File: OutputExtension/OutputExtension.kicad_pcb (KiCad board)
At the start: 2 copper layers, 34 parts, among them P1 CONN_01X04, P2 CONN_01X04, P3 CONN_01X04, P4 CONN_01X08, P5 CONN_01X08, Q1 IRL640, Q2 IRL640, Q3 IRL640, Q4 IRL640, Q5 IRL640, Q6 IRL640, Q7 IRL640, Q8 IRL640, U1 PCF8574

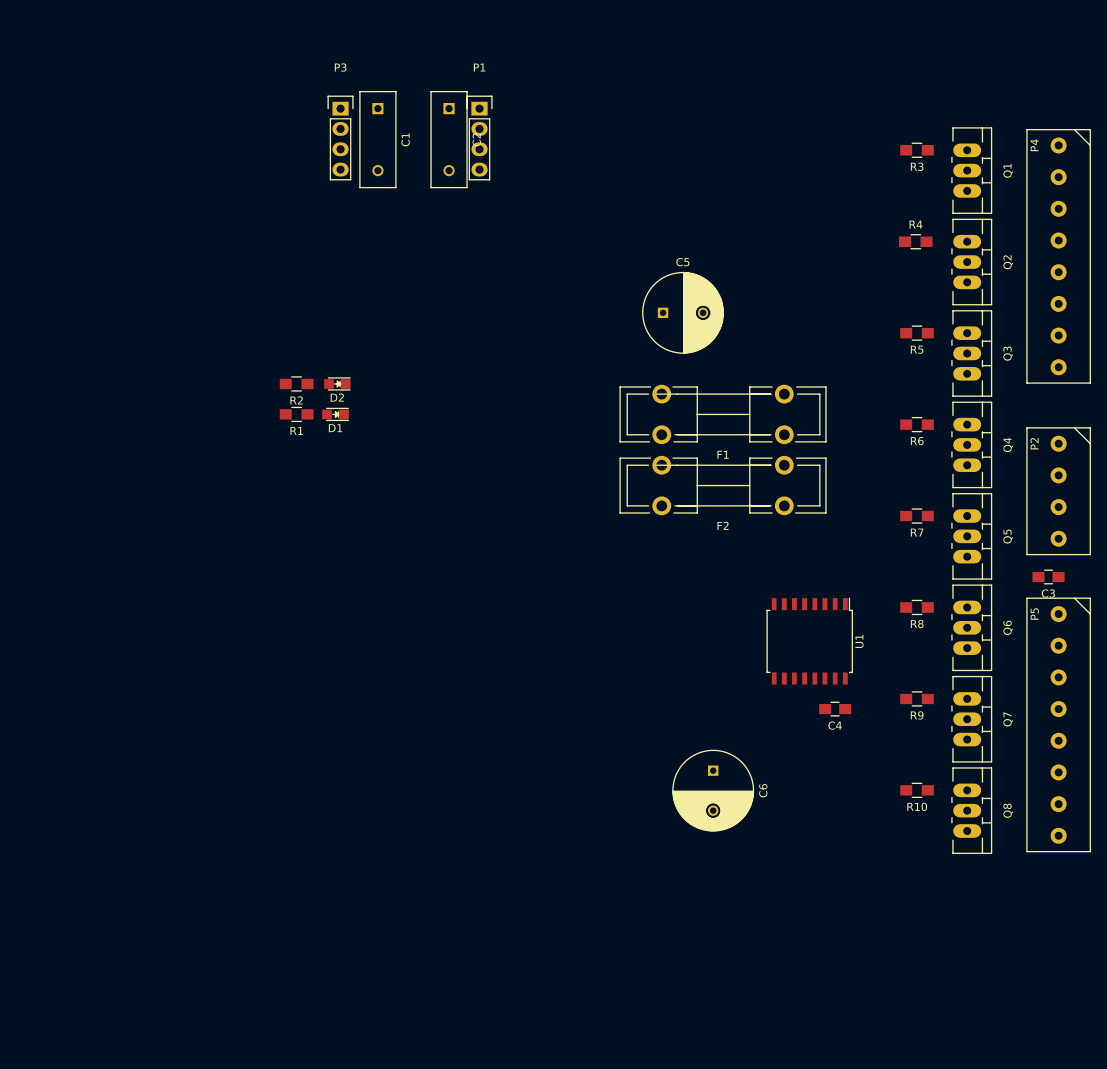
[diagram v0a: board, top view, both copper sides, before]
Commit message: Output extension looks good. Diodes still missing
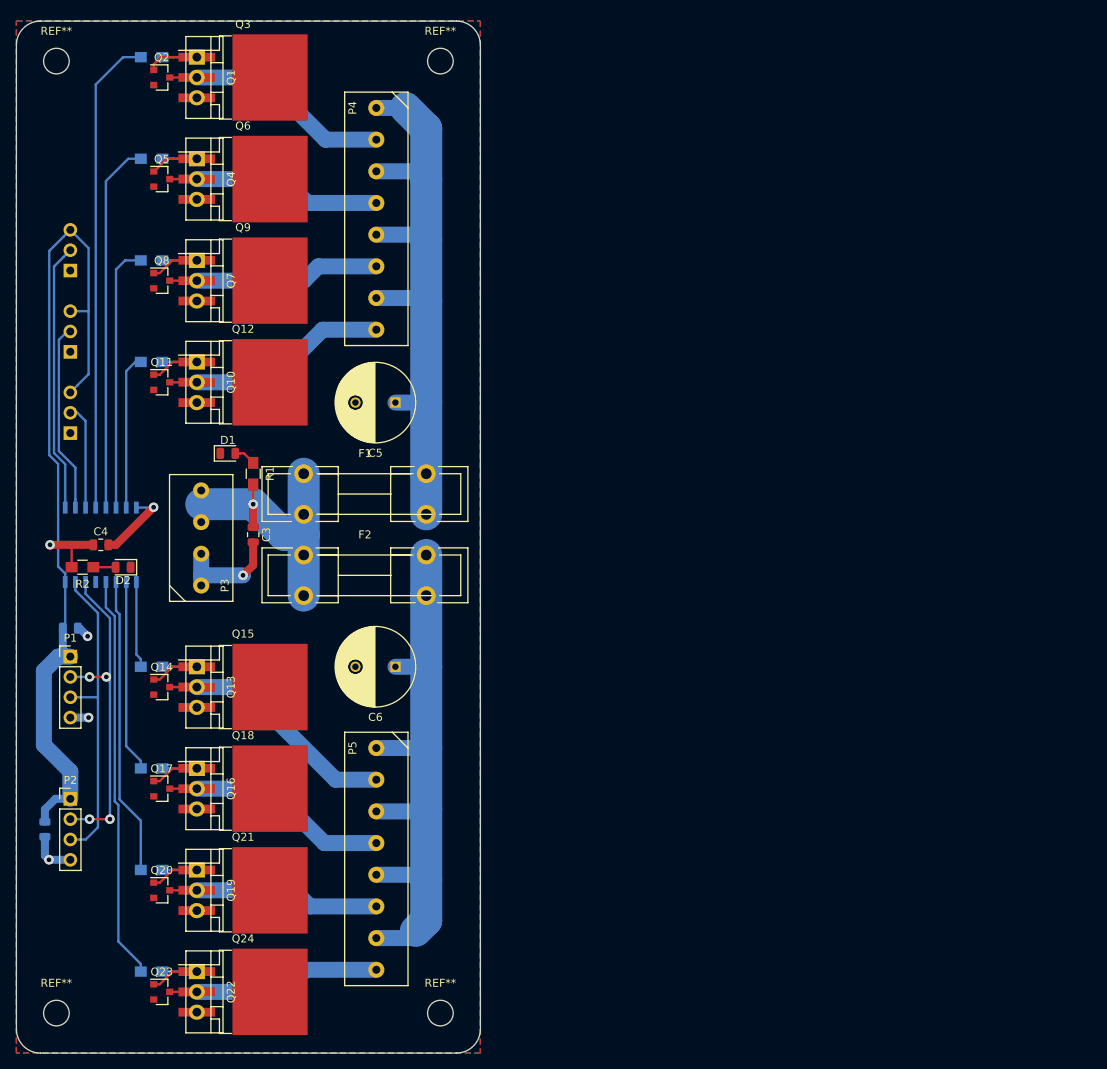
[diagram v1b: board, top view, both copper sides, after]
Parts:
- added JP1: A0, Connector_PinHeader_2.54mm:PinHeader_1x03_P2.54mm_Vertical, B.Cu at (84.7, 72.2)
- added JP2: A1, Connector_PinHeader_2.54mm:PinHeader_1x03_P2.54mm_Vertical, B.Cu at (84.7, 82.3)
- added JP3: A2, Connector_PinHeader_2.54mm:PinHeader_1x03_P2.54mm_Vertical, B.Cu at (84.7, 92.5)
- added Q10: IRL640, Package_TO_SOT_THT:TO-220-3_Vertical, F.Cu at (100.6, 83.6)
- added Q11: BSS138, Package_TO_SOT_SMD:SOT-23, F.Cu at (96.2, 86.2)
- added Q12: 35N15, Package_TO_SOT_SMD:TO-263-3_TabPin2, F.Cu at (106.3, 86.2)
- added Q13: IRL640, Package_TO_SOT_THT:TO-220-3_Vertical, F.Cu at (100.6, 121.7)
- added Q14: BSS138, Package_TO_SOT_SMD:SOT-23, F.Cu at (96.2, 124.2)
- added Q15: 35N15, Package_TO_SOT_SMD:TO-263-3_TabPin2, F.Cu at (106.3, 124.2)
- added Q16: IRL640, Package_TO_SOT_THT:TO-220-3_Vertical, F.Cu at (100.6, 134.4)
- added Q17: BSS138, Package_TO_SOT_SMD:SOT-23, F.Cu at (96.2, 136.9)
- added Q18: 35N15, Package_TO_SOT_SMD:TO-263-3_TabPin2, F.Cu at (106.3, 136.9)
- added Q19: IRL640, Package_TO_SOT_THT:TO-220-3_Vertical, F.Cu at (100.6, 147.1)
- added Q20: BSS138, Package_TO_SOT_SMD:SOT-23, F.Cu at (96.2, 149.7)
- added Q21: 35N15, Package_TO_SOT_SMD:TO-263-3_TabPin2, F.Cu at (106.3, 149.7)
- added Q22: IRL640, Package_TO_SOT_THT:TO-220-3_Vertical, F.Cu at (100.6, 159.8)
- added Q23: BSS138, Package_TO_SOT_SMD:SOT-23, F.Cu at (96.2, 162.3)
- added Q24: 35N15, Package_TO_SOT_SMD:TO-263-3_TabPin2, F.Cu at (106.3, 162.3)
- added Q9: 35N15, Package_TO_SOT_SMD:TO-263-3_TabPin2, F.Cu at (106.3, 73.5)
- added REF**: MountingHole_3.2mm_M3_ISO14580, MountingHole:MountingHole_3.2mm_M3_ISO14580, F.Cu at (83.0, 165.0)
- added REF**: MountingHole_3.2mm_M3_ISO14580, MountingHole:MountingHole_3.2mm_M3_ISO14580, F.Cu at (131.0, 165.0)
- added REF**: MountingHole_3.2mm_M3_ISO14580, MountingHole:MountingHole_3.2mm_M3_ISO14580, F.Cu at (131.0, 46.0)
- added REF**: MountingHole_3.2mm_M3_ISO14580, MountingHole:MountingHole_3.2mm_M3_ISO14580, F.Cu at (83.0, 46.0)
- C1, C2: value 100n -> 1u; footprint Capacitors_ThroughHole:C_Disc_D12_P7.75 -> Capacitor_SMD:C_0805_2012Metric; moved to B.Cu
- C3: value 330n -> 1u; footprint Capacitors_SMD:C_0805_HandSoldering -> Capacitor_SMD:C_0805_2012Metric
- C4: value 100n -> 1u; footprint Capacitors_SMD:C_0805_HandSoldering -> Capacitor_SMD:C_0805_2012Metric
- D1, D2: footprint LEDs:LED-0805 -> LED_SMD:LED_0805_2012Metric
- P1: footprint Pin_Headers:Pin_Header_Straight_1x04 -> Connector_PinHeader_2.54mm:PinHeader_1x04_P2.54mm_Vertical
- P2: footprint my_foots:HT396_4 -> Connector_PinHeader_2.54mm:PinHeader_1x04_P2.54mm_Vertical
- P3: footprint Pin_Headers:Pin_Header_Straight_1x04 -> myStuff:HT396_4
- P4, P5: footprint my_foots:HT396_8 -> myStuff:HT396_8
- Q1, Q4, Q7: footprint TO_SOT_Packages_THT:TO-220_Neutral123_Vertical_LargePads -> Package_TO_SOT_THT:TO-220-3_Vertical
- Q2, Q5, Q8: value IRL640 -> BSS138; footprint TO_SOT_Packages_THT:TO-220_Neutral123_Vertical_LargePads -> Package_TO_SOT_SMD:SOT-23
- Q3, Q6: value IRL640 -> 35N15; footprint TO_SOT_Packages_THT:TO-220_Neutral123_Vertical_LargePads -> Package_TO_SOT_SMD:TO-263-3_TabPin2
- R10, R3, R4, R5, R6, R7, R8, R9, U1: moved to B.Cu
- moved P2 127.6 mm to (84.7, 138.2), turned to 0 degrees
- moved Q8 120.5 mm to (96.2, 73.5), turned to 0 degrees
- moved Q7 112.1 mm to (100.6, 70.9)
- moved Q5 110.1 mm to (96.2, 60.8), turned to 0 degrees
- moved Q6 106.5 mm to (106.3, 60.8), turned to 0 degrees
- moved Q2 103.3 mm to (96.2, 48.0), turned to 0 degrees
- moved C2 103.3 mm to (81.6, 142.0)
- moved Q4 102.7 mm to (100.6, 58.2)
- moved C3 99.6 mm to (107.6, 105.2), turned to 270 degrees
- moved R10 98.3 mm to (94.9, 159.8)
- moved R9 98.0 mm to (94.9, 147.1)
- moved R8 97.8 mm to (94.9, 134.4)
- moved R7 97.5 mm to (94.9, 121.7)
- moved Q1 97.3 mm to (100.6, 45.5)
- moved Q3 96.9 mm to (106.3, 48.0), turned to 0 degrees
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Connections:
- P2 pad 1: GND -> +5V
- P2 pad 2: GND -> /I2C_SCL
- P2 pad 3: +24V -> /I2C_SDA
- P2 pad 4: +24V -> GND
- P3 pad 1: +5V -> GND
- P3 pad 2: /I2C_SCL -> GND
- P3 pad 3: /I2C_SDA -> +24V
- P3 pad 4: GND -> +24V
- Q2 pad 1: Net-(Q2-Pad1) -> Net-(Q1-Pad1)
- Q2 pad 2: /powerChannel1/DRAIN -> GND
- Q2 pad 3: GND -> /powerChannel0/DRAIN
- Q3 pad 1: Net-(Q3-Pad1) -> Net-(Q1-Pad1)
- Q3 pad 2: /powerChannel2/DRAIN -> /powerChannel0/DRAIN
- Q4 pad 2: /powerChannel3/DRAIN -> /powerChannel1/DRAIN
- Q5 pad 1: Net-(Q5-Pad1) -> Net-(Q4-Pad1)
- Q5 pad 2: /powerChannel4/DRAIN -> GND
- Q5 pad 3: GND -> /powerChannel1/DRAIN
- Q6 pad 1: Net-(Q6-Pad1) -> Net-(Q4-Pad1)
- Q6 pad 2: /powerChannel5/DRAIN -> /powerChannel1/DRAIN
- Q7 pad 2: /powerChannel6/DRAIN -> /powerChannel2/DRAIN
- Q8 pad 1: Net-(Q8-Pad1) -> Net-(Q7-Pad1)
- Q8 pad 2: /powerChannel7/DRAIN -> GND
- Q8 pad 3: GND -> /powerChannel2/DRAIN
- R10 pad 1: Net-(Q8-Pad1) -> Net-(Q22-Pad1)
- R4 pad 1: Net-(Q2-Pad1) -> Net-(Q4-Pad1)
- R5 pad 1: Net-(Q3-Pad1) -> Net-(Q7-Pad1)
- R6 pad 1: Net-(Q4-Pad1) -> Net-(Q10-Pad1)
- R7 pad 1: Net-(Q5-Pad1) -> Net-(Q13-Pad1)
- R8 pad 1: Net-(Q6-Pad1) -> Net-(Q16-Pad1)
- R9 pad 1: Net-(Q7-Pad1) -> Net-(Q19-Pad1)
- U1 pad 1: GND -> /A0
- U1 pad 13: (no net) -> Net-(U1-Pad13)
- U1 pad 2: GND -> /A1
- U1 pad 3: GND -> /A2
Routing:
- net +5V: track 0.00 -> 116.2 mm, vias 0 -> 1
- net Net-(C5-Pad1): track 0.00 -> 78.9 mm
- net Net-(C6-Pad1): track 0.00 -> 75.8 mm
- net /powerChannel0/CTRL: track 0.00 -> 59.9 mm
- net +24V: track 0.00 -> 54.2 mm, vias 0 -> 1
- net /powerChannel7/CTRL: track 0.00 -> 50.5 mm
- net /powerChannel1/CTRL: track 0.00 -> 46.3 mm
- net /I2C_SCL: track 0.00 -> 41.3 mm, vias 0 -> 4
- net /I2C_SDA: track 0.00 -> 39.4 mm
- net /powerChannel6/CTRL: track 0.00 -> 37.3 mm
- net /A0: track 0.00 -> 33.6 mm
- net /powerChannel2/CTRL: track 0.00 -> 33.3 mm
- net GND: track 0.00 -> 33.3 mm, vias 0 -> 5
- net /powerChannel4/DRAIN: track 0.00 -> 30.6 mm
- net /powerChannel0/DRAIN: track 0.00 -> 29.0 mm
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- added copper zone on B.Cu, net GND
- added copper zone on F.Cu, net GND
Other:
- board outline added: 58 x 129 mm
- net class Default: clearance 0.2 -> 0.3; trace_width 0.25 -> 0.3; via_dia 0.6 -> 1.2; via_drill 0.4 -> 0.6
- rule trace_clearance: 0.2 -> 0.3
- rule trace_min: 0.2 -> 0.3
- rule via_min_drill: 0.3 -> 0.6
- rule via_min_size: 0.4 -> 1.2

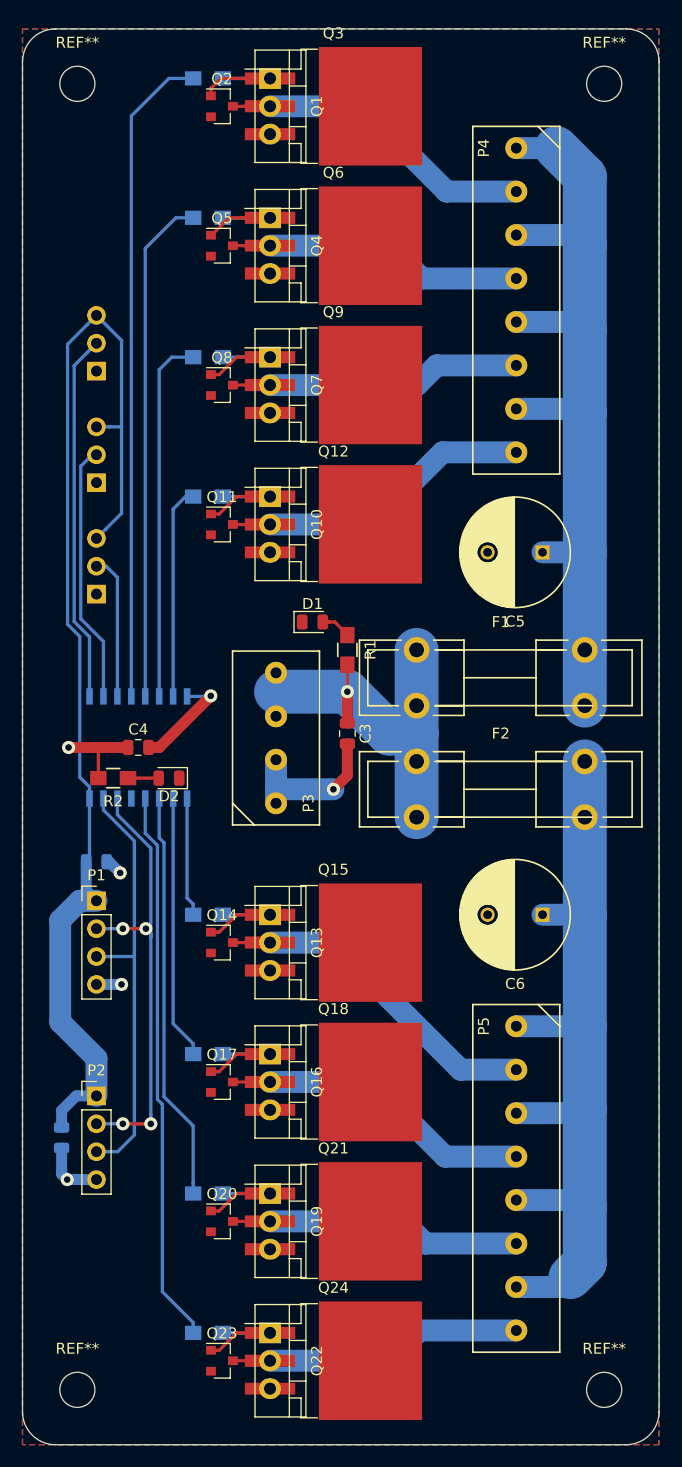
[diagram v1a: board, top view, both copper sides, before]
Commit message: Add diodes
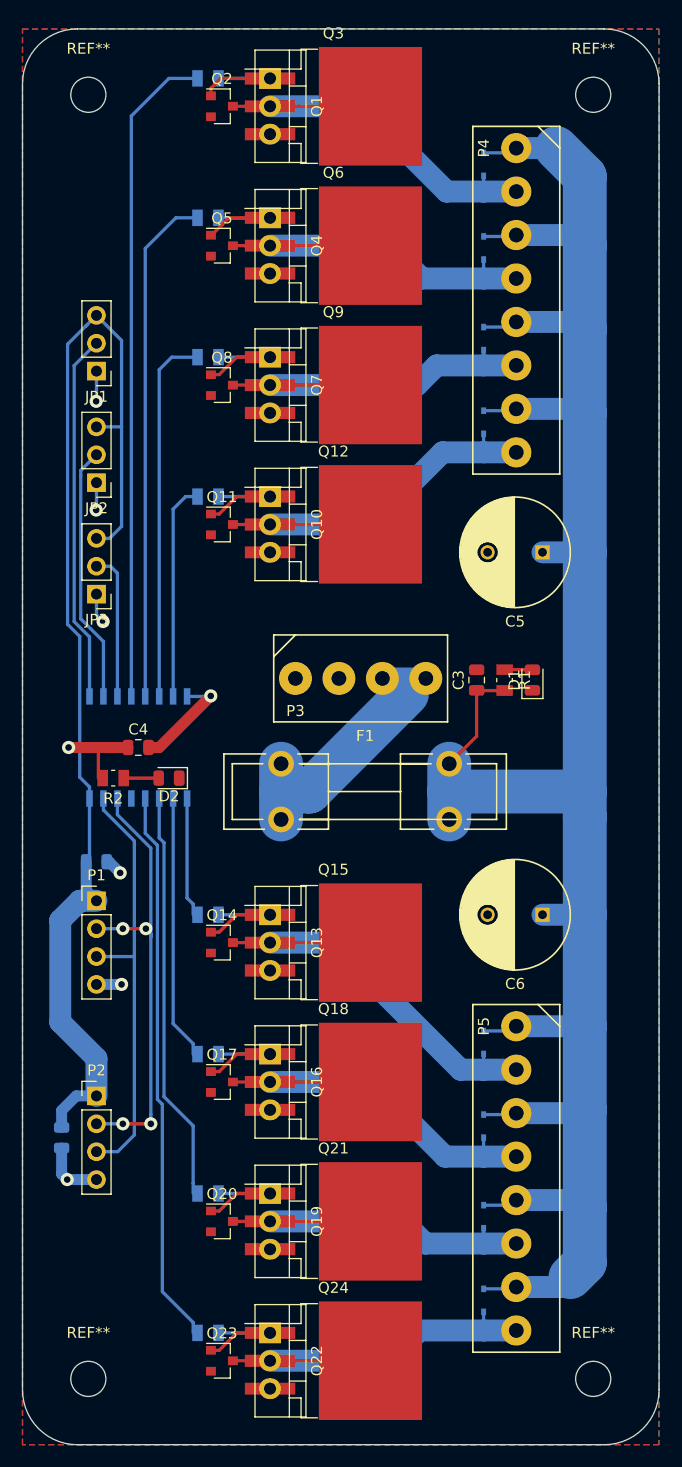
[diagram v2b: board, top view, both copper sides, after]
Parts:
- removed F2: FUSE, Fuse_Holders_and_Fuses:Fuseholder5x20_horiz_open_lateral_Type-II
- removed the REF** at (83.0, 165.0)
- removed the REF** at (131.0, 165.0)
- removed the REF** at (131.0, 46.0)
- removed the REF** at (83.0, 46.0)
- added D10: B5819WS, Diode_SMD:D_SOD-323, B.Cu at (120.0, 156.8)
- added D3: B5819WS, Diode_SMD:D_SOD-323, B.Cu at (120.0, 53.3)
- added D4: B5819WS, Diode_SMD:D_SOD-323, B.Cu at (120.0, 61.0)
- added D5: B5819WS, Diode_SMD:D_SOD-323, B.Cu at (120.0, 69.2)
- added D6: B5819WS, Diode_SMD:D_SOD-323, B.Cu at (120.0, 76.8)
- added D7: B5819WS, Diode_SMD:D_SOD-323, B.Cu at (120.0, 133.3)
- added D8: B5819WS, Diode_SMD:D_SOD-323, B.Cu at (120.0, 141.0)
- added D9: B5819WS, Diode_SMD:D_SOD-323, B.Cu at (120.0, 149.2)
- added REF**: MountingHole_3.2mm_M3, MountingHole:MountingHole_3.2mm_M3, F.Cu at (84.0, 164.0)
- added REF**: MountingHole_3.2mm_M3, MountingHole:MountingHole_3.2mm_M3, F.Cu at (130.0, 164.0)
- added REF**: MountingHole_3.2mm_M3, MountingHole:MountingHole_3.2mm_M3, F.Cu at (130.0, 47.0)
- added REF**: MountingHole_3.2mm_M3, MountingHole:MountingHole_3.2mm_M3, F.Cu at (84.0, 47.0)
- JP1, JP2, JP3: moved to F.Cu
- R1, R10, R2, R3, R4, R5, R6, R7, R8, R9: footprint Resistors_SMD:R_0805_HandSoldering -> Resistor_SMD:R_0805_2012Metric
- moved D1 20.7 mm to (124.5, 100.3), turned to 90 degrees
- moved F1 16.1 mm to (109.2, 110.5)
- moved R1 14.6 mm to (121.9, 100.3)
- moved C3 12.7 mm to (119.4, 100.3), turned to 90 degrees
- moved P3 7.73 mm to (102.9, 104.1), turned to 0 degrees
- turned JP1 to 180 degrees
- turned JP2 to 180 degrees
- turned JP3 to 180 degrees
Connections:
- C5 pad 1: Net-(C5-Pad1) -> +24V
- C6 pad 1: Net-(C6-Pad1) -> +24V
- F1 pad 1: +24V -> Net-(F1-Pad1)
- F1 pad 2: Net-(C5-Pad1) -> +24V
- P3 pad 3: +24V -> Net-(F1-Pad1)
- P3 pad 4: +24V -> Net-(F1-Pad1)
- P4 pad 1: Net-(C5-Pad1) -> +24V
- P4 pad 3: Net-(C5-Pad1) -> +24V
- P4 pad 5: Net-(C5-Pad1) -> +24V
- P4 pad 7: Net-(C5-Pad1) -> +24V
- P5 pad 1: Net-(C6-Pad1) -> +24V
- P5 pad 3: Net-(C6-Pad1) -> +24V
- P5 pad 5: Net-(C6-Pad1) -> +24V
- P5 pad 7: Net-(C6-Pad1) -> +24V
- U1 pad 13: Net-(U1-Pad13) -> (no net)
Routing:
- net +24V: track 54.2 -> 212.3 mm, vias 1 -> 0
- net Net-(C5-Pad1): track 78.9 -> 0.00 mm
- net Net-(C6-Pad1): track 75.8 -> 0.00 mm
- net Net-(F1-Pad1): track 0.00 -> 24.2 mm
- net /powerChannel1/DRAIN: track 27.1 -> 37.9 mm
- net /powerChannel5/DRAIN: track 28.6 -> 39.5 mm
- net /powerChannel7/DRAIN: track 27.0 -> 37.8 mm
- net /powerChannel3/DRAIN: track 28.5 -> 39.4 mm
- net /powerChannel4/DRAIN: track 30.6 -> 41.2 mm
- net /powerChannel0/DRAIN: track 29.0 -> 39.6 mm
- net /powerChannel2/DRAIN: track 26.6 -> 37.1 mm
- net /powerChannel6/DRAIN: track 26.7 -> 37.2 mm
- net GND: track 33.3 -> 27.5 mm, vias 5 -> 7
- net +5V: track 116.2 -> 117.1 mm
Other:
- outline, holes or cut-outs redrawn

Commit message: Output extension ready for fab
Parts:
- renumbered REF** to M1, REF** to M2, REF** to M3, REF** to M4
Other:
- board text added: "24 V"
- board text added: "24 V in"
- board text added: "5 V"
- board text added: "A0"
- board text added: "A1"
- board text added: "A2"
- board text added: "GND"
- board text added: "I2C IN"
- board text added: "I2C OUT"
- board text added: "Open collector out"
- board text added: "Q0"
- board text added: "Q1"
- board text added: "Q2"
- board text added: "Q3"
- board text added: "Q4"
- board text added: "Q5"
- board text added: "Q6"
- board text added: "Q7"
- board text added: "SCL"
- board text added: "SDA"

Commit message: .4 mm traces
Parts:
- moved C2 7.70 mm to (82.3, 134.4), turned to 180 degrees
- moved C1 2.92 mm to (82.3, 118.5), turned to 180 degrees
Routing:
- net +24V: track 212.3 -> 362.3 mm
- net /powerChannel0/DRAIN: track 39.6 -> 65.3 mm
- net Net-(F1-Pad1): track 24.2 -> 33.9 mm
- net /powerChannel7/DRAIN: track 37.8 -> 46.4 mm
- net /powerChannel6/DRAIN: track 37.2 -> 45.0 mm
- net /powerChannel3/DRAIN: track 39.4 -> 46.1 mm
- net /powerChannel5/DRAIN: track 39.5 -> 45.8 mm
- net /I2C_SCL: track 41.3 -> 47.3 mm
- net /powerChannel4/DRAIN: track 41.2 -> 45.9 mm
- net /I2C_SDA: track 39.4 -> 36.3 mm
- net /powerChannel2/DRAIN: track 37.1 -> 40.1 mm
- net /powerChannel1/DRAIN: track 37.9 -> 40.9 mm
- net GND: track 27.5 -> 26.1 mm, vias 7 -> 8
- net +5V: track 117.1 -> 115.9 mm
- net /A0: track 33.6 -> 34.5 mm
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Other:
- net class Default: clearance 0.3 -> 0.4; trace_width 0.3 -> 0.4
- rule trace_clearance: 0.3 -> 0.4
- rule trace_min: 0.3 -> 0.4

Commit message: Fabbed version
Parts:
- removed M1, M2, M3, M4: MountingHole_3.2mm_M3, MountingHole:MountingHole_3.2mm_M3
- added F2: FUSE, myStuff:littlefuse_154_smd, F.Cu at (115.6, 110.5)
- added REF**: MountingHole_3.2mm_M3, MountingHole:MountingHole_3.2mm_M3, F.Cu at (84.0, 164.0)
- added REF**: MountingHole_3.2mm_M3, MountingHole:MountingHole_3.2mm_M3, F.Cu at (130.0, 164.0)
- added REF**: MountingHole_3.2mm_M3, MountingHole:MountingHole_3.2mm_M3, F.Cu at (130.0, 47.0)
- added REF**: MountingHole_3.2mm_M3, MountingHole:MountingHole_3.2mm_M3, F.Cu at (84.0, 47.0)
- F1: footprint Fuse_Holders_and_Fuses:Fuseholder5x20_horiz_open_lateral_Type-II -> myStuff:LBL_FUSE
- moved D1 5.54 mm to (119.0, 101.5), turned to 270 degrees
- moved C3 4.89 mm to (124.1, 101.5), turned to 270 degrees
- moved F1 1.27 mm to (110.5, 110.5)
- moved R1 1.22 mm to (121.6, 101.5), turned to 90 degrees
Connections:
- U1 pad 13: (no net) -> Net-(U1-Pad13)
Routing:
- net +24V: track 362.3 -> 350.4 mm, vias 0 -> 1
- net Net-(F1-Pad1): track 33.9 -> 31.1 mm
- net GND: track 26.1 -> 27.8 mm, vias 8 -> 9

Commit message: silkscreen
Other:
- board text added: "Open drain out"
- board text removed: "Open collector out"
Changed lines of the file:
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@@
     (effects (font (size 1 1) (thickness 0.2)))
   )
-  (gr_text "Open collector out" (at 116.84 151.13 90) (layer F.SilkS)
+  (gr_text "Open drain out" (at 116.84 151.13 90) (layer F.SilkS)
     (effects (font (size 1.5 1.5) (thickness 0.35)))
   )
@@
     (effects (font (size 1 1) (thickness 0.2)))
   )
-  (gr_text "Open collector out" (at 116.84 71.12 90) (layer F.SilkS)
+  (gr_text "Open drain out" (at 116.84 71.12 90) (layer F.SilkS)
     (effects (font (size 1.5 1.5) (thickness 0.35)))
   )
